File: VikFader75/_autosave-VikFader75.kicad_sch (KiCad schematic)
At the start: 15 parts, among them J1 vik-module-connector, J2 Conn_01x06_Pin, Q1 DMG2305UX, U1 ADS1115IDGS

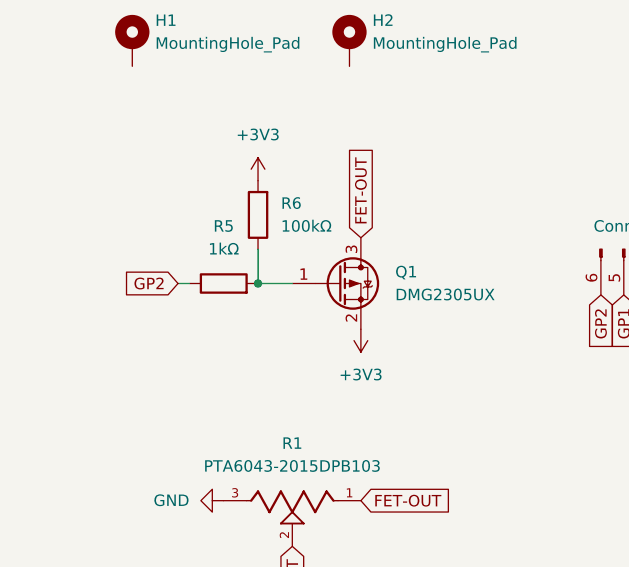
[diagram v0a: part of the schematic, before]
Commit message: Updated 75 to new MOSFET design
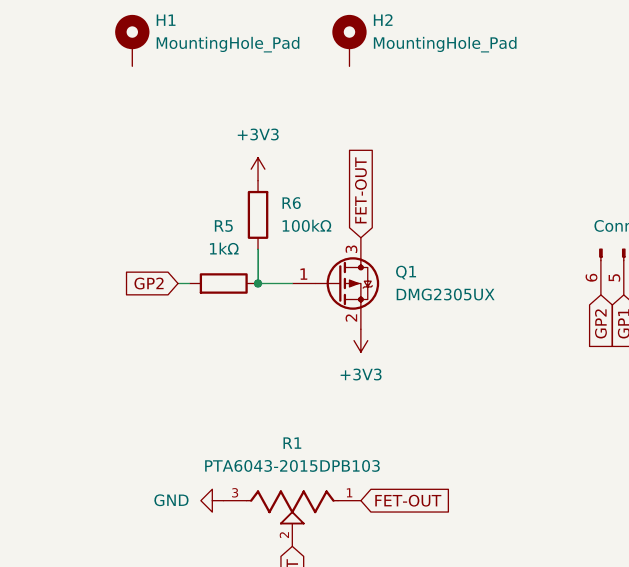
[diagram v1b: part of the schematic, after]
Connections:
- net GP2: now also R5.2; no longer R5.1
- net at Q1.1 (G), R6.1: now also R5.1; no longer R5.2
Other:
- moved on the sheet: R5
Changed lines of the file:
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@@
 	(symbol
 		(lib_id "Device:R")
-		(at 39.37 90.17 90)
+		(at 39.37 90.17 270)
+		(mirror x)
 		(unit 1)
 		(exclude_from_sim no)
@@
 		(on_board yes)
 		(dnp no)
-		(fields_autoplaced yes)
 		(property "Reference" "R5"
 			(at 39.37 83.82 90)
